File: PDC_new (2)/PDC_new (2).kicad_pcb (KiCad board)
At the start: 2 copper layers, 156.5 x 145.5 mm, 83 parts, among them J1 Conn_01x02_Pin, J10 Conn_01x02_Pin, J11 XT90PW(2+2)-M.G.Y, J12 Conn_01x02_Pin, J13 Conn_01x02_Pin, J14 Conn_01x02_Pin, J15 Conn_01x02_Pin, J2 Conn_01x02_Pin, J3 Conn_01x02_Pin, J4 Conn_01x02_Pin, J5 Conn_01x02_Pin, J6 Conn_01x02_Pin, J7 Conn_01x02_Pin, J8 Conn_01x02_Pin, J9 Conn_01x02_Pin, Q2 IRF540NSTRLPBF, U1 TPSI3050QDWZRQ1, U10 LM393LVDR, U11 IPB017N10N5ATMA1, U12 IPB017N10N5ATMA1, U14 IPB017N10N5ATMA1, U2 TPSI3050QDWZRQ1, U4 74HC74, U5 URB4805LD-60WR3, U6 IPB017N10N5ATMA1, U7 TLC555CDR, U8 SN74HC08D, U9 SN74HC14DR

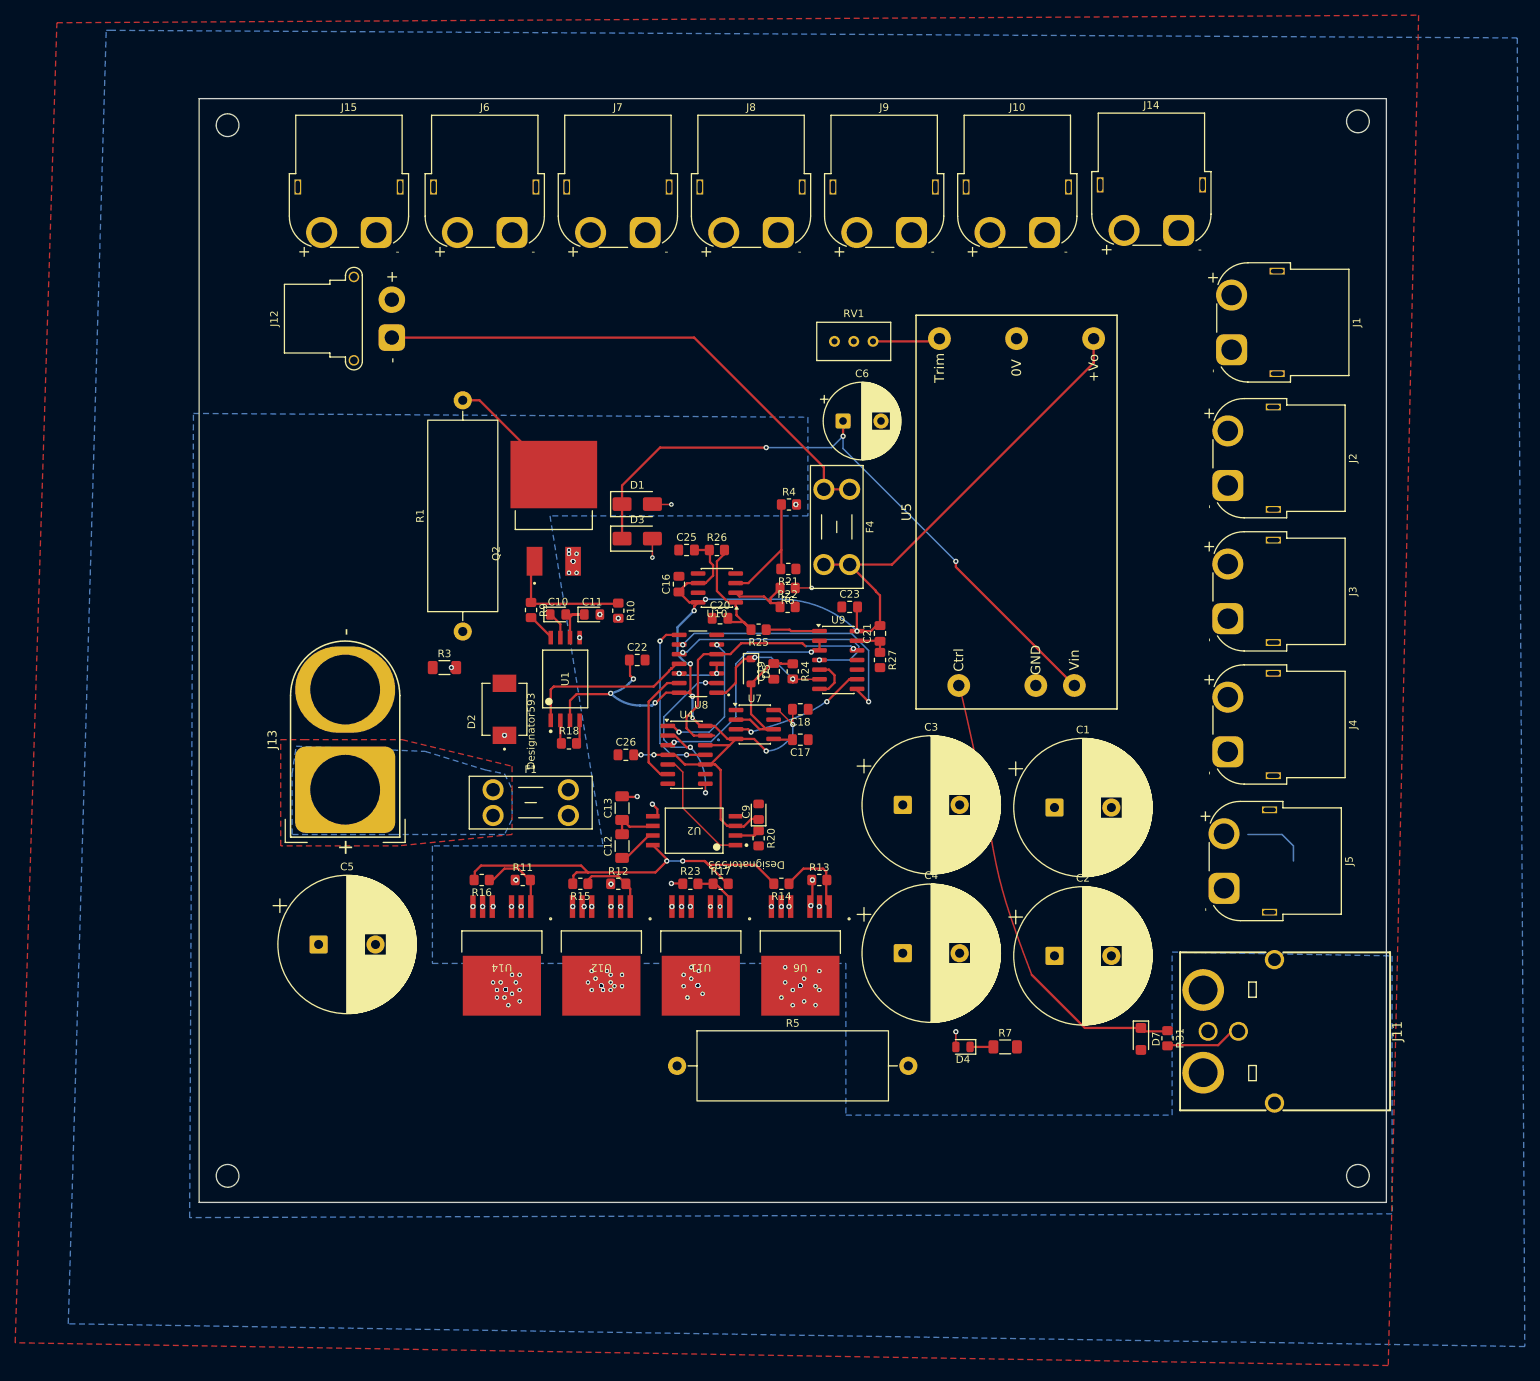
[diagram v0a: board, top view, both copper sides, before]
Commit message: pcb: clean up vias, widen power tracks, silkscreen and branding
- Remove 54 duplicate stacked vias (under MOSFET tabs and at Q2) and one
  BUS+ via violating hole-to-hole clearance
- Widen PRE_DRAIN to 2.0 mm, BUCK_IN to 1.0 mm, and the U5 -> F4 -> J12
  5 V power path to 2.0 mm; refill zones
- Remove silkscreen outlines and hide reference labels on all parts except
  ICs and capacitors; keep connector +/- markings
- Add cathode markings for D1-D5 and D7
- Add "NEXUS PDB V2.0" / "Designed by: Lakshmeesha and Jayanth" silkscreen
- Add project fp-lib-table for PDC_new (2)
- README: document the open main-current-through-vias issue and other
  open items, update status and project layout

DRC: 0 errors, 0 unconnected items.

Co-Authored-By: Claude Opus 5.5 <noreply@anthropic.com>
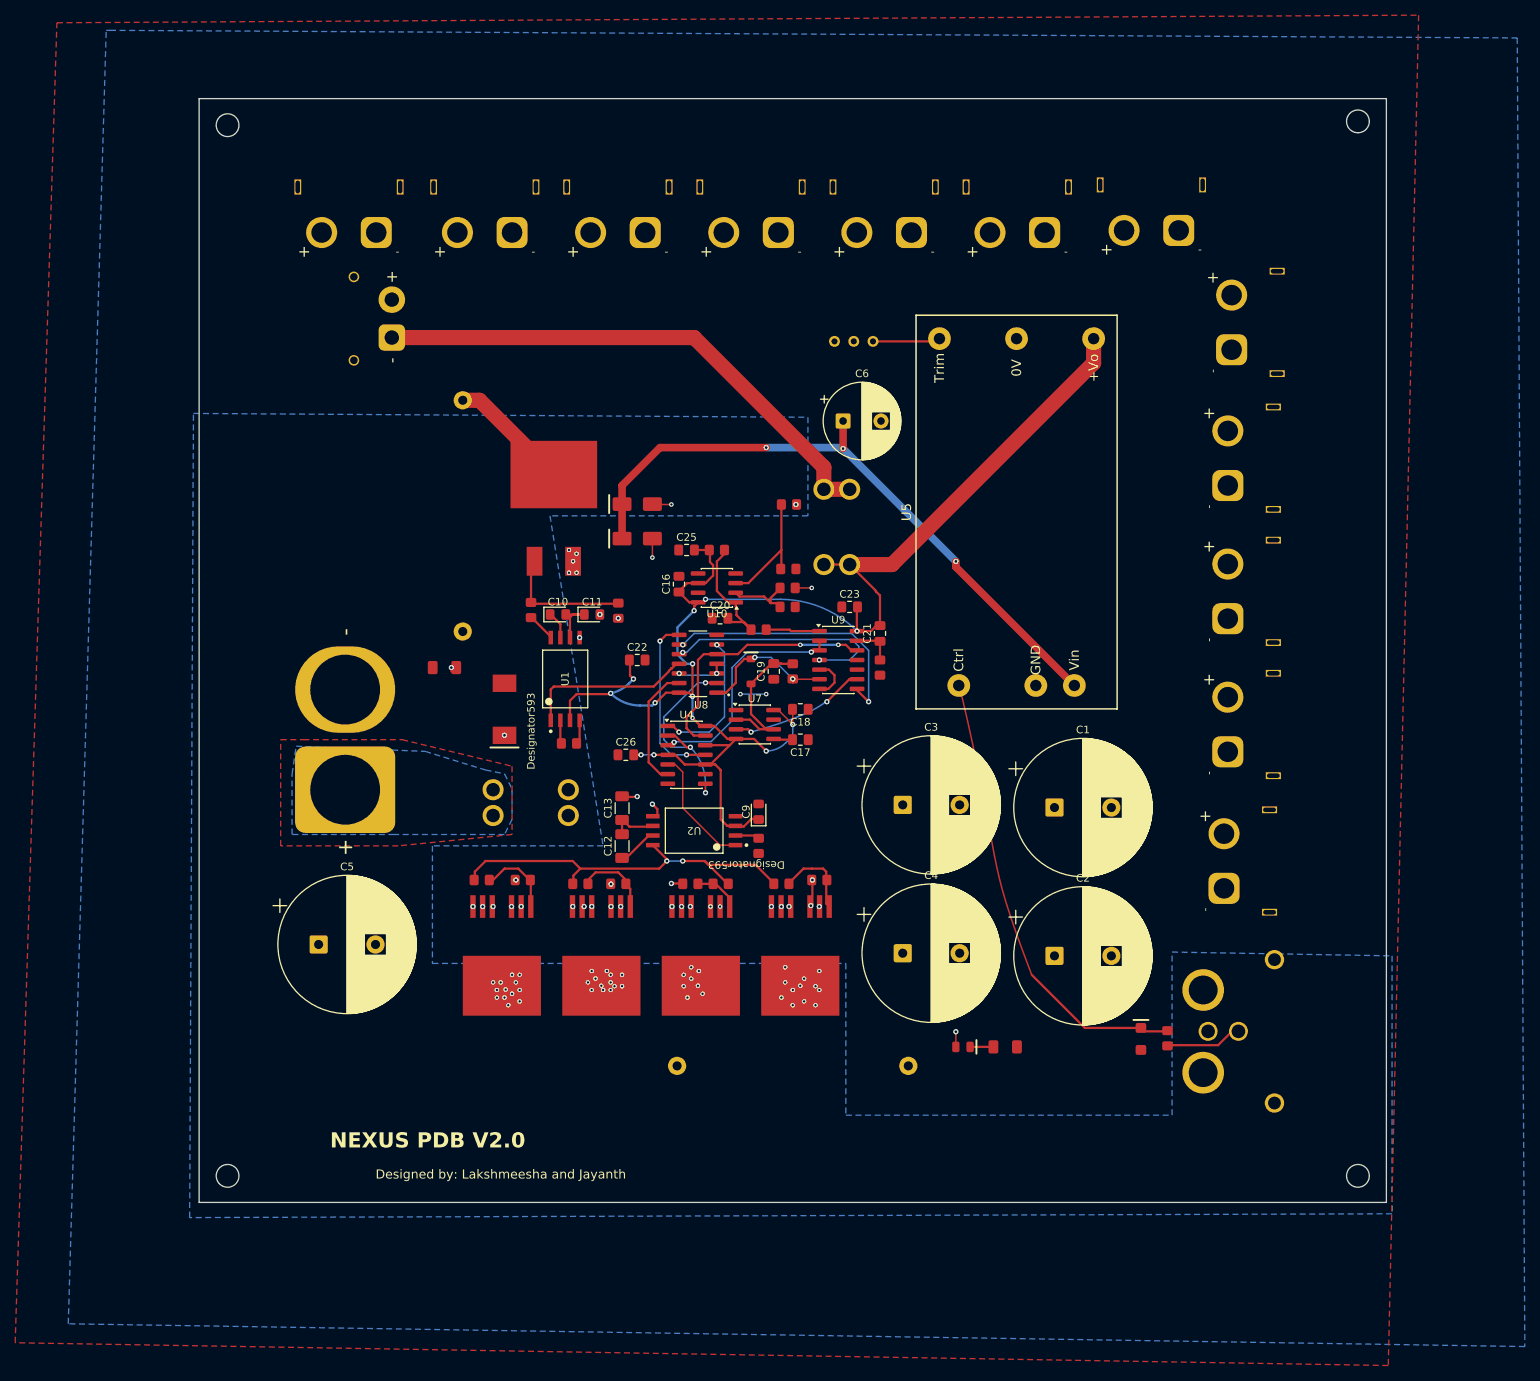
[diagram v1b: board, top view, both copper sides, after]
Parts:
- moved R20 1.00 mm to (306.5, 225.5)
- moved R27 1.00 mm to (322.5, 202.0)
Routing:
- net (no net): track 8.62 -> 0.00 mm
- net GND: track 8.84 -> 12.2 mm, vias 0 -> 2
- net /reset_N: track 36.2 -> 34.6 mm, vias 1 -> 2
- net /reset_rc: track 4.67 -> 5.58 mm
- net /GATE_U12: track 9.40 -> 10.1 mm
- net /GATE_MAIN: track 53.4 -> 52.7 mm
- net /BUCK_IN: track 86.3 -> 85.7 mm
- net /BUS+: vias 43 -> 37
- net /BATT+: vias 99 -> 50
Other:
- board text added: "Designed by: Lakshmeesha and Jayanth"
- board text added: "NEXUS PDB V2.0"
